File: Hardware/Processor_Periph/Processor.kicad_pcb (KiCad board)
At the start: 4 copper layers, 123.2 x 78.5 mm, 100 parts, among them J1 5V, J2 UART0, J3 USB_OTG, J4 JTAGICE3-SWD, J5 PIOA, J6 PIOB, J7 PIOC, J8 PIOD, Q1 BSSB06NE, Q2 BSSB06NE, Q3 BSSB06NE, Q4 BSSB06NE, SW1 PB, SW2 PB, SW3 ~RST, U1 TXS0102, U2 ATSAM4E16E, U3 3.0V, U4 LM3671, U5 PRTR5V0U2X, Y1 32.768kHz, Y2 12MHz

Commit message: Assigned some footprints, finished BOM
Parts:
- removed J1: 5V, FritzLib:ConnectorSMD-1x3
- removed J2: UART0, FritzLib:ConnectorSMD-1x4
- removed J3: USB_OTG, FritzLib:conn_usb_B_micro_smd
- removed J4: JTAGICE3-SWD, FritzLib:ConnectorMicromatch-10
- removed J5: PIOA, FritzLib:ConnectorSMD-40
- removed J6: PIOB, FritzLib:ConnectorSMD-24
- removed J7: PIOC, FritzLib:ConnectorSMD-40
- removed J8: PIOD, FritzLib:ConnectorSMD-40
- removed JP1: 5V_SEL, FritzLib:ConnectorSMD-1x3
- removed L1: 10uH, FritzLib:Inductor_3mmx3mm
- removed L2: 2.2uH, Inductors:Inductor_1212
- removed Q1, Q2, Q3, Q4: BSSB06NE, TO_SOT_Packages_SMD:SOT-23
- removed Y1: 32.768kHz, FritzLib:FC-135R
- removed Y2: 12MHz, Crystals:Crystal_HC49-SD_SMD
- added C29: 100nF, Capacitors_SMD:C_0603, F.Cu at (112.5, 75.4)
- added C42: 100nF, Capacitors_SMD:C_0603, F.Cu at (127.7, 74.7)
- added C43: 100nF, Capacitors_SMD:C_0603, F.Cu at (132.3, 69.8)
- added C44: 10uF, Capacitors_SMD:C_0805, F.Cu at (77.2, 104.0)
- added C45: 100nF, Capacitors_SMD:C_0603, F.Cu at (98.6, 103.1)
- added C46: 100nF, Capacitors_SMD:C_0603, F.Cu at (103.7, 98.1)
- added C47: 100nF, Capacitors_SMD:C_0603, F.Cu at (122.2, 70.0)
- added C48: 100nF, Capacitors_SMD:C_0603, F.Cu at (92.0, 106.1)
- added C49: 4.7uF, Capacitors_SMD:C_0805, F.Cu at (88.5, 94.1)
- added C50: 100nF, Capacitors_SMD:C_0603, F.Cu at (98.6, 98.1)
- added C51: 100nF, Capacitors_SMD:C_0603, F.Cu at (111.0, 86.7)
- added C52: 2.2uF, Capacitors_SMD:C_0805, F.Cu at (117.1, 64.8)
- added C53: 10uF, Capacitors_SMD:C_0805, F.Cu at (104.2, 77.7)
- added C54: 100nF, Capacitors_SMD:C_0603, F.Cu at (105.9, 93.0)
- added C55: 100nF, Capacitors_SMD:C_0603, F.Cu at (122.7, 74.9)
- added C56: 100nF, Capacitors_SMD:C_0603, F.Cu at (127.3, 69.8)
- added C57: 10nF, Capacitors_SMD:C_0603, F.Cu at (144.5, 64.8)
- added C58: 100nF, Capacitors_SMD:C_0603, F.Cu at (114.2, 80.3)
- added C59: 100nF, Capacitors_SMD:C_0603, F.Cu at (119.3, 80.1)
- added C60: 100nF, Capacitors_SMD:C_0603, F.Cu at (80.4, 114.4)
- added C61: 100nF, Capacitors_SMD:C_0603, F.Cu at (85.5, 109.5)
- added D6: PMEG6030ETP, FritzLib:SOD-128, F.Cu at (59.9, 114.4)
- added J10: JTAGICE3-SWD, Pin_Headers:Pin_Header_Straight_2x05_Pitch1.27mm_SMD, F.Cu at (77.3, 67.6)
- added R23: 100k, Resistors_SMD:R_0603, F.Cu at (141.0, 69.7)
- added R24: 0R, Resistors_SMD:R_0603, F.Cu at (102.0, 108.0)
- added R25: 2.2k, Resistors_SMD:R_0603, F.Cu at (134.4, 99.3)
- added R26: 10k, Resistors_SMD:R_0603, F.Cu at (147.9, 74.6)
- added R27: 0R, Resistors_SMD:R_0603, F.Cu at (127.5, 94.4)
- added R28: 10k, Resistors_SMD:R_0603, F.Cu at (119.9, 100.0)
- added R29: 2.2k, Resistors_SMD:R_0603, F.Cu at (144.4, 74.6)
- added R30: 27R, Resistors_SMD:R_0603, F.Cu at (105.5, 112.9)
- added R31: 27R, Resistors_SMD:R_0603, F.Cu at (112.7, 106.4)
- added R32: 27R, Resistors_SMD:R_0603, F.Cu at (124.0, 94.8)
- added R33: 27R, Resistors_SMD:R_0603, F.Cu at (120.6, 95.1)
- added R34: 0R, Resistors_SMD:R_0603, F.Cu at (132.7, 84.5)
- added R35: 0R, Resistors_SMD:R_0603, F.Cu at (137.5, 79.6)
- added R36: 1R, Resistors_SMD:R_0603, F.Cu at (124.0, 99.7)
- added R37: 10k, Resistors_SMD:R_0603, F.Cu at (108.9, 112.6)
- added R38: 1.5K, Resistors_SMD:R_0603, F.Cu at (137.5, 113.9)
- added R39: 10k, Resistors_SMD:R_0603, F.Cu at (141.6, 109.0)
- added R40: 10k, Resistors_SMD:R_0603, F.Cu at (145.2, 104.0)
- added R41: 10k, Resistors_SMD:R_0603, F.Cu at (138.2, 109.0)
- added R42: 27R, Resistors_SMD:R_0603, F.Cu at (133.3, 114.0)
- added R43: 10k, Resistors_SMD:R_0603, F.Cu at (141.6, 104.1)
- added R44: 10k, Resistors_SMD:R_0603, F.Cu at (145.2, 99.1)
- added R45: 10k, Resistors_SMD:R_0603, F.Cu at (130.0, 114.0)
- added R46: 10k, Resistors_SMD:R_0603, F.Cu at (138.2, 104.1)
- added R47: 10k, Resistors_SMD:R_0603, F.Cu at (133.9, 109.1)
- added R48: 10k, Resistors_SMD:R_0603, F.Cu at (136.3, 89.4)
- added R49: 2.2k, Resistors_SMD:R_0603, F.Cu at (127.4, 104.2)
- added R50: 2.2k, Resistors_SMD:R_0603, F.Cu at (139.8, 89.4)
- added R51: 2.2k, Resistors_SMD:R_0603, F.Cu at (134.7, 94.3)
- added R52: 2.2k, Resistors_SMD:R_0603, F.Cu at (119.5, 109.8)
- added R53: 150R, Resistors_SMD:R_0805, F.Cu at (91.1, 87.8)
- added R54: 2.2k, Resistors_SMD:R_0603, F.Cu at (112.4, 116.2)
- added R55: 2.2k, Resistors_SMD:R_0603, F.Cu at (123.4, 104.6)
- added R56: 2.2k, Resistors_SMD:R_0603, F.Cu at (142.9, 84.5)
- added R57: 2.2k, Resistors_SMD:R_0603, F.Cu at (131.0, 94.4)
- added R58: 10k, Resistors_SMD:R_0603, F.Cu at (116.0, 109.8)
- added R59: 150R, Resistors_SMD:R_0805, F.Cu at (100.0, 77.9)
- added R60: 2.2k, Resistors_SMD:R_0603, F.Cu at (136.2, 74.7)
- added R61: 2.2k, Resistors_SMD:R_0603, F.Cu at (127.4, 99.3)
- added R62: 2.2k, Resistors_SMD:R_0603, F.Cu at (144.6, 79.5)
- added R63: 2.2k, Resistors_SMD:R_0603, F.Cu at (119.5, 104.9)
- added R64: 10k, Resistors_SMD:R_0603, F.Cu at (139.4, 84.5)
- added R65: 2.2k, Resistors_SMD:R_0603, F.Cu at (112.5, 111.3)
- added R66: 2.2k, Resistors_SMD:R_0603, F.Cu at (108.9, 107.7)
- added R67: 2.2k, Resistors_SMD:R_0603, F.Cu at (141.0, 79.6)
- added R68: 2.2k, Resistors_SMD:R_0603, F.Cu at (132.8, 89.4)
- added R69: 150R, Resistors_SMD:R_0805, F.Cu at (95.6, 80.9)
- added R70: 10k, Resistors_SMD:R_0603, F.Cu at (136.0, 84.5)
- added R71: 10k, Resistors_SMD:R_0603, F.Cu at (116.0, 104.9)
- added R72: 2.2k, Resistors_SMD:R_0603, F.Cu at (145.1, 108.9)
- added R73: 2.2k, Resistors_SMD:R_0603, F.Cu at (130.4, 109.1)
- added R74: 2.2k, Resistors_SMD:R_0603, F.Cu at (141.7, 99.2)
- added R75: 2.2k, Resistors_SMD:R_0603, F.Cu at (146.5, 84.4)
- added R76: 150R, Resistors_SMD:R_0805, F.Cu at (112.6, 65.0)
- added R77: 2.2k, Resistors_SMD:R_0603, F.Cu at (134.7, 104.2)
- added R78: 2.2k, Resistors_SMD:R_0603, F.Cu at (138.1, 99.2)
- added R79: 2.2k, Resistors_SMD:R_0603, F.Cu at (123.1, 114.4)
- added R80: 2.2k, Resistors_SMD:R_0603, F.Cu at (131.1, 104.2)
- added R81: 27R, Resistors_SMD:R_0603, F.Cu at (146.7, 89.3)
- added R82: 27R, Resistors_SMD:R_0603, F.Cu at (141.5, 94.3)
- added R83: 27R, Resistors_SMD:R_0603, F.Cu at (126.9, 109.1)
- added R84: 27R, Resistors_SMD:R_0603, F.Cu at (146.7, 94.2)
- added R85: 27R, Resistors_SMD:R_0603, F.Cu at (119.3, 114.7)
- added R86: 27R, Resistors_SMD:R_0603, F.Cu at (138.2, 94.3)
- added R87: 27R, Resistors_SMD:R_0603, F.Cu at (143.3, 89.4)
- added R88: 27R, Resistors_SMD:R_0603, F.Cu at (123.0, 109.5)
- added R89: 27R, Resistors_SMD:R_0603, F.Cu at (130.9, 99.3)
- added R90: 27R, Resistors_SMD:R_0603, F.Cu at (116.0, 114.7)
- added R91: 27R, Resistors_SMD:R_0603, F.Cu at (148.1, 79.5)
- added R92: 0R, Resistors_SMD:R_0603, F.Cu at (126.6, 114.0)
- added TP10: 1V2, Measurement_Points:Test_Point_Keystone_5019_Minature, F.Cu at (86.4, 88.4)
- added TP11: XOUT_32, Measurement_Points:Test_Point_Keystone_5019_Minature, F.Cu at (93.8, 75.0)
- added TP12: XIN_32, Measurement_Points:Test_Point_Keystone_5019_Minature, F.Cu at (79.3, 98.3)
- added TP13: MCU_XIN, Measurement_Points:Test_Point_Keystone_5019_Minature, F.Cu at (90.0, 82.0)
- added TP14: PHY_XIN, Measurement_Points:Test_Point_Keystone_5019_Minature, F.Cu at (102.1, 65.6)
- added TP9: 1V8, Measurement_Points:Test_Point_Keystone_5019_Minature, F.Cu at (107.9, 65.6)
- added U7: DP83848C, Housings_QFP:LQFP-48_7x7mm_Pitch0.5mm, F.Cu at (53.5, 95.8)
- added U8: ATSAM4E16E, Housings_QFP:TQFP-144_20x20mm_Pitch0.5mm, F.Cu at (59.8, 75.6)
- added U9: 3.0V, TO_SOT_Packages_SMD:SOT-23, F.Cu at (88.5, 75.3)
- C10, C11: value 27pF -> 1uF; footprint Capacitors_SMD:C_0603 -> Capacitors_SMD:C_0805
- C13, C17, C22, C7: value 10nF -> 100nF
- C14, C16, C21, C33, C37: value 100nF -> 10nF
- C19, C20: value 12pF -> 100nF
- C2: value 10nF -> 4.7uF; footprint Capacitors_SMD:C_0603 -> Capacitors_SMD:C_0805
- C23: value 100nF -> 4.7uF; footprint Capacitors_SMD:C_0603 -> Capacitors_SMD:C_0805
- C31, C40: value 4.7uF -> 100nF; footprint Capacitors_SMD:C_0805 -> Capacitors_SMD:C_0603
- C34: value 2.2uF -> 100nF; footprint Capacitors_SMD:C_0805 -> Capacitors_SMD:C_0603
- C4: value 4.5nF -> 3.9pF
- C41: value 10uF -> 10nF; footprint Capacitors_SMD:C_0805 -> Capacitors_SMD:C_0603
- C5: value 100nF -> 3.9pF
- C6: value 100nF -> 4.5nF
- C9: value 100nF -> 10uF; footprint Capacitors_SMD:C_0603 -> Capacitors_SMD:C_0805
- D1, D2, D3, D4, D5: footprint LEDs:LED_0805 -> Diodes_SMD:D_0805
- R1: value 1M -> 10k; footprint Capacitors_SMD:C_0603 -> Resistors_SMD:R_0603
- R10, R9: value 10k -> 150R; footprint Capacitors_SMD:C_0603 -> Resistors_SMD:R_0805
- R11, R6: value 27R -> 10k; footprint Capacitors_SMD:C_0603 -> Resistors_SMD:R_0603
- R12, R18: value 10k -> 100k; footprint Capacitors_SMD:C_0603 -> Resistors_SMD:R_0603
- R13: value 10k -> 4.87k; footprint Capacitors_SMD:C_0603 -> Resistors_SMD:R_0603
- R14: value 150R -> 100k; footprint Capacitors_SMD:C_0805 -> Resistors_SMD:R_0603
- R15, R3, R4, R5: footprint Capacitors_SMD:C_0603 -> Resistors_SMD:R_0603
- R16, R20: value 10k -> 49.9R; footprint Capacitors_SMD:C_0603 -> Resistors_SMD:R_0603
- R17, R21: value 150R -> 49.9R; footprint Capacitors_SMD:C_0805 -> Resistors_SMD:R_0603
- R19, R22: value 150R -> 10k; footprint Capacitors_SMD:C_0805 -> Resistors_SMD:R_0603
- R2: value 10k -> 1M; footprint Capacitors_SMD:C_0603 -> Resistors_SMD:R_0603
- R7: value 27R -> 150R; footprint Capacitors_SMD:C_0603 -> Resistors_SMD:R_0805
- R8: value 1R -> 10k; footprint Capacitors_SMD:C_0603 -> Resistors_SMD:R_0603
- SW1: value PB -> ~RST
- SW3: value ~RST -> PB
- TP1: footprint Measurement_Points:Measurement_Point_Round-SMD-Pad_Small -> Measurement_Points:Test_Point_Keystone_5019_Minature
- TP2: value ERASE -> U0_RXD; footprint Measurement_Points:Measurement_Point_Round-SMD-Pad_Small -> Measurement_Points:Test_Point_Keystone_5019_Minature
- TP3: value U0_RXD -> LED_SPEED; footprint Measurement_Points:Measurement_Point_Round-SMD-Pad_Small -> Measurement_Points:Test_Point_Keystone_5019_Minature
- TP4: value JTAG_SEL -> ERASE; footprint Measurement_Points:Measurement_Point_Round-SMD-Pad_Small -> Measurement_Points:Test_Point_Keystone_5019_Minature
- TP5: value TST -> JTAG_SEL; footprint Measurement_Points:Measurement_Point_Round-SMD-Pad_Small -> Measurement_Points:Test_Point_Keystone_5019_Minature
- TP6: value 5V -> TST; footprint Measurement_Points:Measurement_Point_Round-SMD-Pad_Small -> Measurement_Points:Test_Point_Keystone_5019_Minature
- TP7: value 3V3 -> 5V; footprint Measurement_Points:Measurement_Point_Round-SMD-Pad_Small -> Measurement_Points:Test_Point_Keystone_5019_Minature
- TP8: value 1V2 -> 3V3; footprint Measurement_Points:Measurement_Point_Round-SMD-Pad_Small -> Measurement_Points:Test_Point_Keystone_5019_Minature
- U2: value ATSAM4E16E -> LM3671; footprint Housings_QFP:TQFP-144_20x20mm_Pitch0.5mm -> TO_SOT_Packages_SMD:SOT-23-5
- U3: value 3.0V -> S25FL127S; footprint TO_SOT_Packages_SMD:SOT-23 -> Housings_SOIC:SOIC-8_3.9x4.9mm_Pitch1.27mm
- U4: value LM3671 -> PRTR5V0U2X; footprint TO_SOT_Packages_SMD:SOT-23-5 -> TO_SOT_Packages_SMD:SOT-143
- U5: value PRTR5V0U2X -> MIC5365; footprint FritzLib:SOT143B -> TO_SOT_Packages_SMD:SOT-23-5
- moved TP4 308.4 mm to (60.6, 109.3)
- moved TP6 306.1 mm to (79.0, 91.9)
- moved TP3 301.2 mm to (72.1, 92.1)
- moved TP7 301.2 mm to (68.4, 101.5)
- moved TP1 299.8 mm to (66.1, 109.3)
- moved TP2 299.6 mm to (101.9, 72.0)
- moved TP8 293.1 mm to (81.3, 85.4)
- moved TP5 288.1 mm to (75.2, 85.4)
- moved D5 106.8 mm to (70.9, 113.8), turned to 0 degrees
- moved R10 104.6 mm to (73.0, 97.9), turned to 0 degrees
- moved U4 99.5 mm to (53.3, 106.2)
- moved SW3 93.0 mm to (87.5, 67.1)
- moved U1 83.1 mm to (95.4, 65.9), turned to 0 degrees
- moved U5 71.0 mm to (62.4, 102.2), turned to 0 degrees
- moved C15 69.8 mm to (100.8, 88.2)
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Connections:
- C1 pad 1: +3V3 -> +5V_UART
- C10 pad 1: /XIN32 -> +3V3
- C11 pad 1: /XOUT32 -> +1V8
- C12 pad 1: +1V2 -> +1V8
- C14 pad 1: +3V3 -> +1V8
- C16 pad 1: +1V2 -> +3V3
- C19 pad 1: /XOUT -> +3V3
- C2 pad 1: +3V3 -> +5V
- C20 pad 1: /XIN -> +1V2
- C21 pad 1: +1V2 -> +3V3
- C30 pad 1: /VDDPLL -> +3V3
- C31 pad 1: Net-(C31-Pad1) -> +3V3
- C32 pad 1: /AREF -> +1V2
- C34 pad 1: +1V2 -> +3V3
- C35 pad 1: +3V3 -> /PFBOUT
- C37 pad 1: Net-(C37-Pad1) -> +3V3
- C38 pad 1: /PE5 -> +3V3
- C39 pad 1: /PE4 -> /PFBOUT
- C4 pad 1: GND -> /XIN32
- C4 pad 2: Net-(C4-Pad2) -> GND
- C40 pad 1: +5V -> +1V2
- C5 pad 1: /VBUS -> /XOUT32
- C6 pad 1: +1V2 -> GND
- C6 pad 2: GND -> Net-(C6-Pad2)
- C7 pad 1: +3V3 -> +5V_USB
- C9 pad 1: +5V_UART -> +3V3
- D1 pad 1: Net-(D1-Pad1) -> GND
- D5 pad 1: GND -> Net-(D5-Pad1)
- R1 pad 1: GND -> +3V3
- R1 pad 2: Net-(C4-Pad2) -> /NVM_~CS
- R10 pad 1: +3V3 -> GND
- R10 pad 2: SWDCLK -> Net-(J4-Pad11)
- R11 pad 1: ~RST -> +1V8
- R11 pad 2: Net-(C37-Pad1) -> Net-(R11-Pad2)
- R12 pad 2: /PE5 -> /MCCDA2
- R13 pad 1: /PE0 -> /RBIAS
- R14 pad 2: Net-(D1-Pad2) -> /MCCDA3
- R15 pad 2: /PE4 -> /MCCDA
- R16 pad 1: /PE1 -> +3V3
- R16 pad 2: GND -> /ETX-
- R17 pad 1: +3V3 -> /ERX-
- R17 pad 2: Net-(D2-Pad2) -> +3V3
- R18 pad 1: /PE2 -> +3V3
- R18 pad 2: GND -> /MCDA0
- R19 pad 2: Net-(D3-Pad2) -> /I2C_SCL
- R2 pad 1: VBUS_DET -> GND
- R2 pad 2: /VBUS -> Net-(C6-Pad2)
- R20 pad 1: /PE3 -> +3V3
- R20 pad 2: GND -> /ETX+
- R21 pad 1: +3V3 -> /ERX-
- R21 pad 2: Net-(D4-Pad2) -> +3V3
- R22 pad 1: Net-(D5-Pad2) -> +3V3
- R22 pad 2: +3V3 -> /I2C_SCL
- R3 pad 2: Net-(R3-Pad2) -> +5V_USB
- R4 pad 1: Net-(R3-Pad2) -> VBUS_DET
- R4 pad 2: GND -> Net-(R4-Pad2)
- R5 pad 1: +3V3 -> Net-(R4-Pad2)
- R5 pad 2: /U0_TXD -> GND
- R6 pad 1: /DD- -> +3V3
- R6 pad 2: /USBD- -> /U0_TXD
- R7 pad 1: /DD+ -> Net-(D1-Pad2)
- R7 pad 2: /USBD+ -> +3V3
- R8 pad 1: /VDDPLL -> +3V3
- R8 pad 2: Net-(C31-Pad1) -> /LDO_EN
- R9 pad 1: +3V3 -> GND
- R9 pad 2: /AREF -> Net-(J4-Pad10)
- SW1 pad 1: /PE4 -> ~RST
- SW2 pad 1: /PE5 -> /SW2
- SW3 pad 1: ~RST -> /SW1
- TP2 pad 1: /ERASE -> /U0_RXD
- TP3 pad 1: /U0_RXD -> /LED_SP
- TP4 pad 1: /JTAG_SEL -> /ERASE
- TP5 pad 1: /TST -> /JTAG_SEL
- TP6 pad 1: +5V -> /TST
- TP7 pad 1: +3V3 -> +5V
- TP8 pad 1: +1V2 -> +3V3
- U2 pad 1: /PD0 -> +5V
- U2 pad 2: VBUS_DET -> GND
- U2 pad 3: +1V2 -> +5V
- U2 pad 4: /PE0 -> +3V3
- U2 pad 5: +3V3 -> Net-(L1-Pad1)
- U3 pad 1: /AREF -> /NVM_~CS
- U3 pad 2: GND -> /NVM_MISO
- U3 pad 3: (no net) -> Net-(U3-Pad3)
- U4 pad 1: +5V -> Net-(C6-Pad2)
- U4 pad 2: GND -> /USBD-
- U4 pad 3: +5V -> /USBD+
- U4 pad 4: +3V3 -> +5V_USB
- U5 pad 1: Net-(C4-Pad2) -> +3V3
- U5 pad 2: /USBD- -> GND
- U5 pad 3: /USBD+ -> /LDO_EN
- U5 pad 4: /VBUS -> Net-(U5-Pad4)
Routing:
- net /USBD-: track 17.3 -> 0.00 mm
- net /USBD+: track 17.3 -> 0.00 mm
- net /DD-: track 3.51 -> 0.00 mm
- net /DD+: track 3.47 -> 0.00 mm
- net GND: track 0.72 -> 0.00 mm
- removed copper zone on B.Cu, net GND
- removed copper zone on F.Cu, net GND
- removed copper zone on In1.Cu, net GND
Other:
- board size 123.2 x 78.5 mm -> 152.4 x 127 mm

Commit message: Started routing PHY
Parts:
- moved R84 276.8 mm to (-125.2, 146.3), turned to 270 degrees
- moved R81 275.7 mm to (-123.7, 143.5), turned to 90 degrees
- moved R91 275.7 mm to (-116.8, 155.7)
- moved R82 270.3 mm to (-123.7, 146.3), turned to 270 degrees
- moved R87 269.5 mm to (-120.7, 143.5), turned to 90 degrees
- moved R34 268.2 mm to (-128.3, 146.3), turned to 270 degrees
- moved R86 264.9 mm to (-122.2, 143.5), turned to 90 degrees
- moved R35 264.2 mm to (-116.8, 151.1), turned to 180 degrees
- moved R27 257.5 mm to (-121.2, 161.0), turned to 90 degrees
- moved R89 256.0 mm to (-120.7, 146.3), turned to 270 degrees
- moved R83 254.5 mm to (-125.2, 143.5), turned to 90 degrees
- moved C47 252.9 mm to (-116.8, 152.7)
- moved R88 247.9 mm to (-122.2, 146.3), turned to 270 degrees
- moved R85 240.6 mm to (-119.1, 146.3), turned to 90 degrees
- moved R90 236.2 mm to (-116.8, 154.2)
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
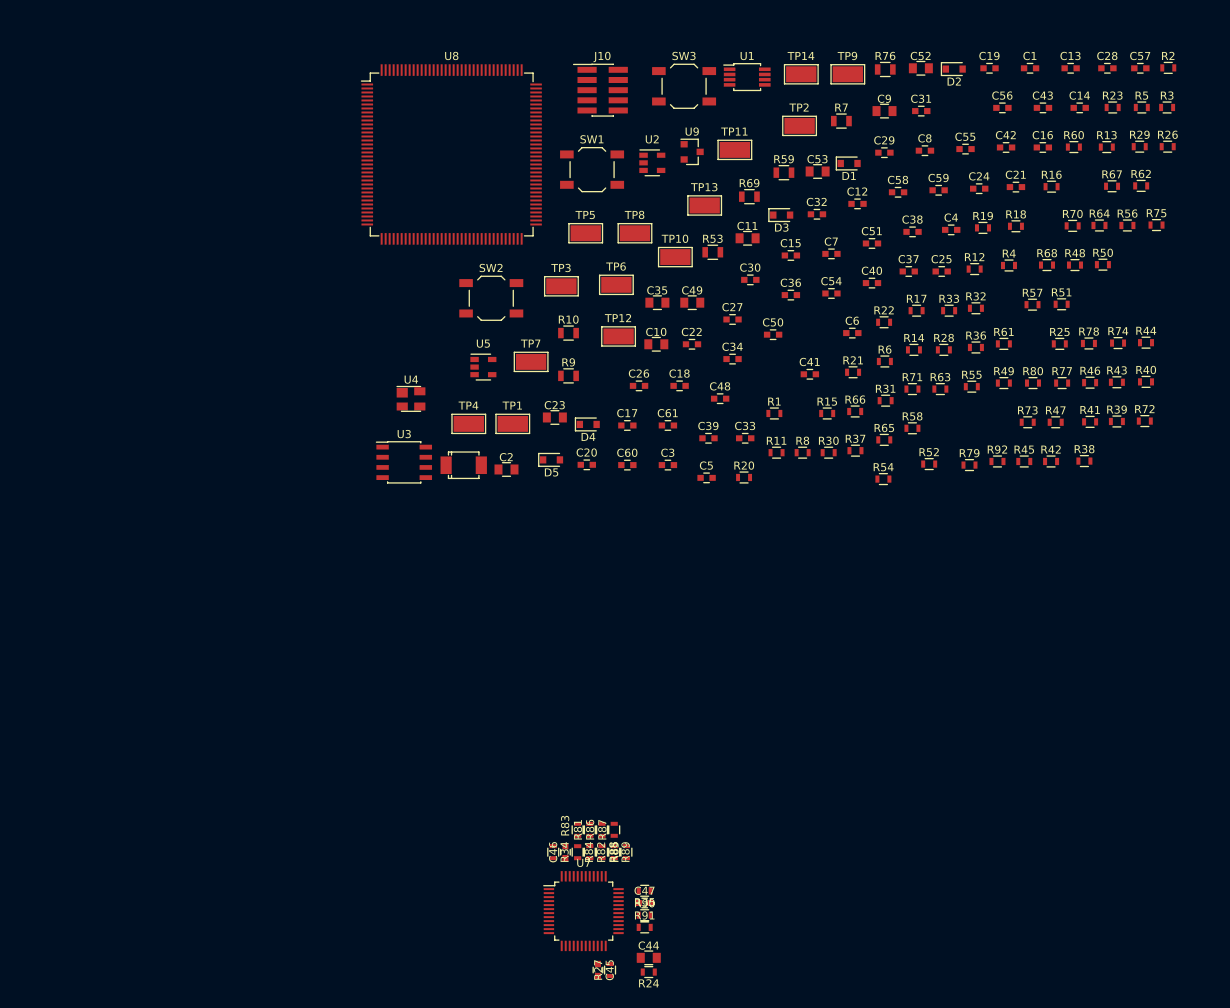
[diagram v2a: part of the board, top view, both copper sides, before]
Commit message: Modified schematic per 5/21 discussion
- Added 2xGPIO expanders & new connectors for interfacing to x4 stepper
motor drivers
- Added buffer for driving PWM outputs to stepper motors
- Added more spare pins & spare pin connectors
- Removed I2C expansion connector (I2C dedicated to GPIO expanders now)
- Cleaned up component values
- Expanded schematic size
- Reannotated entire schematic
- Regenerated schematic PDF

TODO:

- Generate new BOM with new schematic annotation
- Finalize connector footprints
- Begin layout
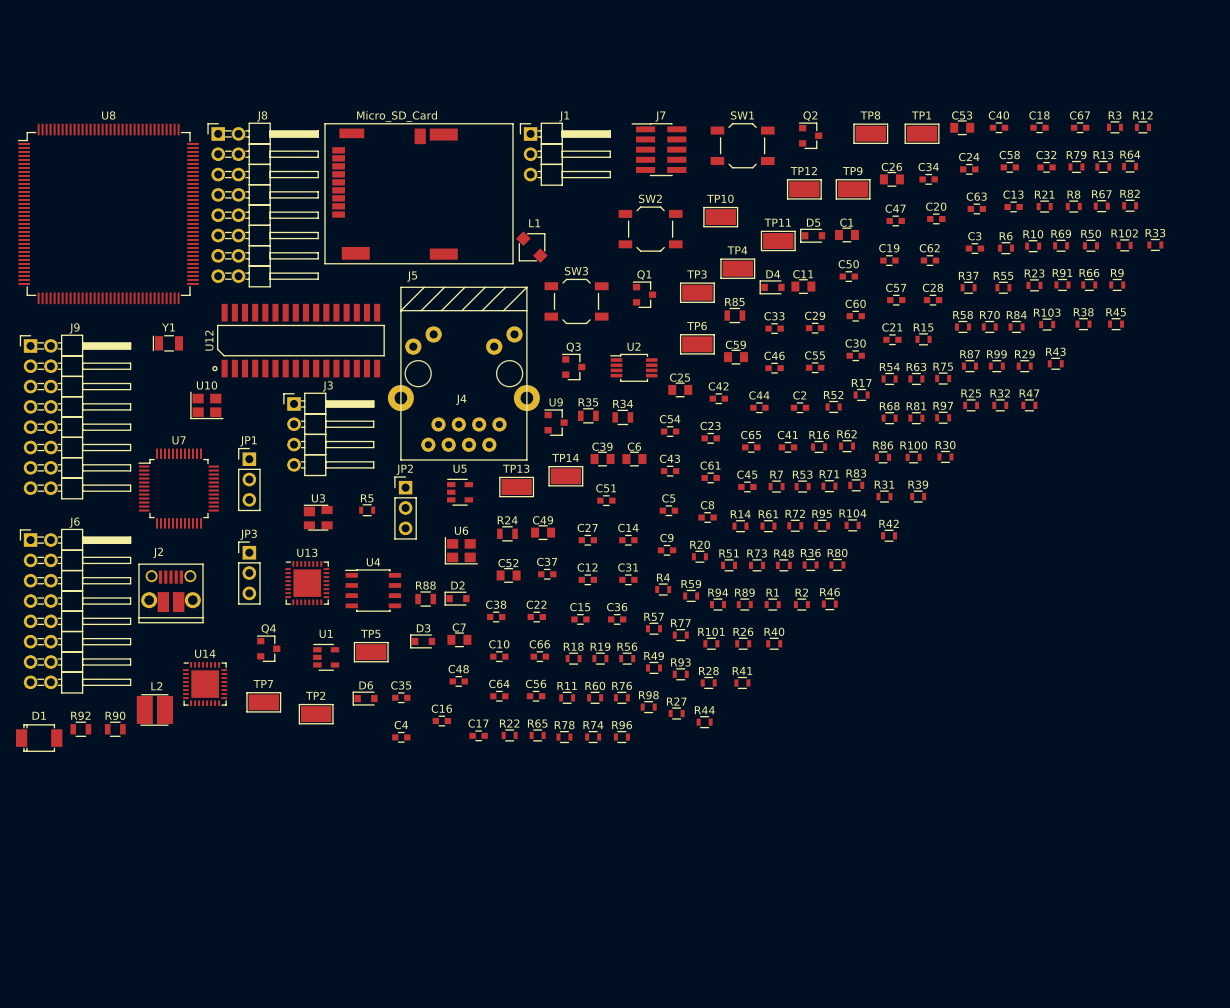
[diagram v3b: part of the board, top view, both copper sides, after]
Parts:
- removed J10: JTAGICE3-SWD, Pin_Headers:Pin_Header_Straight_2x05_Pitch1.27mm_SMD
- added C62: 100nF, Capacitors_SMD:C_0603, F.Cu at (-81.2, 72.3)
- added C63: 100nF, Capacitors_SMD:C_0603, F.Cu at (-75.3, 65.9)
- added C64: 100nF, Capacitors_SMD:C_0603, F.Cu at (-135.0, 126.8)
- added C65: 100nF, Capacitors_SMD:C_0603, F.Cu at (-103.5, 95.7)
- added C66: 100nF, Capacitors_SMD:C_0603, F.Cu at (-129.9, 121.9)
- added C67: 100nF, Capacitors_SMD:C_0603, F.Cu at (-62.4, 55.7)
- added J1: 5V, Pin_Headers:Pin_Header_Angled_1x03_Pitch2.54mm, F.Cu at (-131.1, 56.5)
- added J2: USB_OTG, FritzLib:USB_Micro-B_10103594-0001LF_holes, F.Cu at (-176.1, 113.4)
- added J3: UART0, Pin_Headers:Pin_Header_Angled_1x04_Pitch2.54mm, F.Cu at (-160.7, 90.3)
- added J4: RJ-45_J0006D01BNL, FritzLib:J0006D01BNL, F.Cu at (-147.3, 75.7)
- added J5: Micro_SD_Card, FritzLib:MicroSD-Yamaichi-PJS, F.Cu at (-154.3, 72.2)
- added J6: CONN_SPARE, Pin_Headers:Pin_Header_Angled_2x08_Pitch2.54mm, F.Cu at (-193.6, 107.3)
- added J7: JTAGICE3-SWD, Pin_Headers:Pin_Header_Straight_2x05_Pitch1.27mm_SMD, F.Cu at (-114.8, 58.5)
- added J8: CONN_SPARE, Pin_Headers:Pin_Header_Angled_2x08_Pitch2.54mm, F.Cu at (-170.2, 56.5)
- added J9: CONN_SPARE, Pin_Headers:Pin_Header_Angled_2x08_Pitch2.54mm, F.Cu at (-193.6, 83.0)
- added JP1: VCC_SEL, Pin_Headers:Pin_Header_Straight_1x03_Pitch2.54mm, F.Cu at (-166.3, 97.2)
- added JP2: VCC_SEL, Pin_Headers:Pin_Header_Straight_1x03_Pitch2.54mm, F.Cu at (-146.7, 100.7)
- added JP3: VCC_SEL, Pin_Headers:Pin_Header_Straight_1x03_Pitch2.54mm, F.Cu at (-166.3, 108.9)
- added L1: 2.2uH, FritzLib:CDRH2D14, F.Cu at (-131.9, 69.6)
- added L2: 10uH, FritzLib:Inductor_SMD_3.0mm_x_3.0mm, F.Cu at (-178.3, 128.5)
- added Q1: BSS806NE, TO_SOT_Packages_SMD:SOT-23, F.Cu at (-116.9, 76.6)
- added Q2: BSS806NE, TO_SOT_Packages_SMD:SOT-23, F.Cu at (-96.1, 56.7)
- added Q3: BSS806NE, TO_SOT_Packages_SMD:SOT-23, F.Cu at (-125.7, 85.7)
- added Q4: BSS806NE, TO_SOT_Packages_SMD:SOT-23, F.Cu at (-163.8, 120.9)
- added R100: 10k, Resistors_SMD:R_0603, F.Cu at (-83.2, 96.9)
- added R101: 10k, Resistors_SMD:R_0603, F.Cu at (-108.5, 120.2)
- added R102: 10k, Resistors_SMD:R_0603, F.Cu at (-56.8, 70.4)
- added R103: 10k, Resistors_SMD:R_0603, F.Cu at (-66.5, 80.3)
- added R104: 10k, Resistors_SMD:R_0603, F.Cu at (-90.8, 105.4)
- added R93: 10k, Resistors_SMD:R_0603, F.Cu at (-112.3, 124.1)
- added R94: 10k, Resistors_SMD:R_0603, F.Cu at (-107.7, 115.3)
- added R95: 10k, Resistors_SMD:R_0603, F.Cu at (-94.7, 105.5)
- added R96: 10k, Resistors_SMD:R_0603, F.Cu at (-119.7, 131.9)
- added R97: 10k, Resistors_SMD:R_0603, F.Cu at (-79.5, 92.0)
- added R98: 10k, Resistors_SMD:R_0603, F.Cu at (-116.3, 128.2)
- added R99: 10k, Resistors_SMD:R_0603, F.Cu at (-72.8, 85.5)
- added U10: ASE-25.000MHZ-LC-T, Crystals:Crystal_SMD_3225-4pin_3.2x2.5mm, F.Cu at (-171.6, 90.4)
- added U12: CY7C1018, FritzLib:32-SOJ-300mil, F.Cu at (-159.8, 82.4)
- added U13: TCA6424A, Housings_DFN_QFN:QFN-32-1EP_5x5mm_Pitch0.5mm, F.Cu at (-159.0, 112.7)
- added U14: TCA6424A, Housings_DFN_QFN:QFN-32-1EP_5x5mm_Pitch0.5mm, F.Cu at (-171.8, 125.3)
- added U6: DSC61XX, Crystals:Crystal_SMD_3225-4pin_3.2x2.5mm, F.Cu at (-139.8, 108.6)
- added Y1: 32.768kHz, Crystals:Crystal_SMD_MicroCrystal_CC7V-T1A-2pin_3.2x1.5mm, F.Cu at (-176.3, 82.7)
- C1, C59: value 100nF -> 4.7uF; footprint Capacitors_SMD:C_0603 -> Capacitors_SMD:C_0805
- C10: value 1uF -> 100nF; footprint Capacitors_SMD:C_0805 -> Capacitors_SMD:C_0603
- C13, C17, C32, C36, C45, C56: value 100nF -> 10nF
- C14, C16, C33, C37, C57: value 10nF -> 100nF
- C2, C23: value 4.7uF -> 100nF; footprint Capacitors_SMD:C_0805 -> Capacitors_SMD:C_0603
- C25: value 10nF -> 4.7uF; footprint Capacitors_SMD:C_0603 -> Capacitors_SMD:C_0805
- C26, C39, C7: value 100nF -> 10uF; footprint Capacitors_SMD:C_0603 -> Capacitors_SMD:C_0805
- C3: value 100nF -> 4.5nF
- C35, C44: value 10uF -> 100nF; footprint Capacitors_SMD:C_0805 -> Capacitors_SMD:C_0603
- C4, C5: value 3.9pF -> 100nF
- C6: value 4.5nF -> 1uF; footprint Capacitors_SMD:C_0603 -> Capacitors_SMD:C_0805
- C8: value 100nF -> 3.9pF
- C9: value 10uF -> 3.9pF; footprint Capacitors_SMD:C_0805 -> Capacitors_SMD:C_0603
- D1: value LED -> PMEG6030ETP; footprint Diodes_SMD:D_0805 -> FritzLib:SOD-128
- D6: value PMEG6030ETP -> LED; footprint FritzLib:SOD-128 -> Diodes_SMD:D_0805
- R1, R11, R15, R22, R26, R28, R3, R4, R47, R8: value 10k -> 2.2k
- R10, R9: value 150R -> 2.2k; footprint Resistors_SMD:R_0805 -> Resistors_SMD:R_0603
- R12, R18: value 100k -> 10k
- R13: value 4.87k -> 10k
- R14, R23: value 100k -> 2.2k
- R16, R17, R20, R21: value 49.9R -> 2.2k
- R2: value 1M -> 2.2k
- R24, R34, R35, R92: value 0R -> 150R; footprint Resistors_SMD:R_0603 -> Resistors_SMD:R_0805
- R27: value 0R -> 2.2k
- R30, R31, R32: value 27R -> 2.2k
- R33, R81, R82, R83, R84, R86, R87, R89, R91: value 27R -> 10k
- R36: value 1R -> 0R
- R37: value 10k -> 4.87k
- R38: value 1.5K -> 49.9R
- R39, R41: value 10k -> 49.9R
- R40, R43: value 10k -> 100k
- R42: value 27R -> 49.9R
- R45: value 10k -> 0R
- R49, R56: value 2.2k -> 0R
- R5: value 10k -> 1M
- R50, R55: value 2.2k -> 100k
- R52, R54, R73, R75, R77, R79, R80: value 2.2k -> 10k
- R53: value 150R -> 0R; footprint Resistors_SMD:R_0805 -> Resistors_SMD:R_0603
- R57, R60, R61, R62, R63, R65, R66, R67, R68, R78: value 2.2k -> 27R
- R58, R64, R70, R71: value 10k -> 27R
- R59, R69: value 150R -> 27R; footprint Resistors_SMD:R_0805 -> Resistors_SMD:R_0603
- R7, R76: value 150R -> 10k; footprint Resistors_SMD:R_0805 -> Resistors_SMD:R_0603
- R72: value 2.2k -> 1R
- R74: value 2.2k -> 1.5K
- R85, R88, R90: value 27R -> 150R; footprint Resistors_SMD:R_0603 -> Resistors_SMD:R_0805
- SW1: value ~RST -> PB
- TP1, TP2: footprint Measurement_Points:Test_Point_Keystone_5019_Minature -> FritzLib:Test_Point_Keystone_5019_Minature
- TP10: value 1V2 -> LED_SPEED; footprint Measurement_Points:Test_Point_Keystone_5019_Minature -> FritzLib:Test_Point_Keystone_5019_Minature
- TP11: value XOUT_32 -> ERASE; footprint Measurement_Points:Test_Point_Keystone_5019_Minature -> FritzLib:Test_Point_Keystone_5019_Minature
- TP12: value XIN_32 -> PHY_XIN; footprint Measurement_Points:Test_Point_Keystone_5019_Minature -> FritzLib:Test_Point_Keystone_5019_Minature
- TP13: value MCU_XIN -> JTAG_SEL; footprint Measurement_Points:Test_Point_Keystone_5019_Minature -> FritzLib:Test_Point_Keystone_5019_Minature
- TP14: value PHY_XIN -> TST; footprint Measurement_Points:Test_Point_Keystone_5019_Minature -> FritzLib:Test_Point_Keystone_5019_Minature
- TP3: value LED_SPEED -> 5V; footprint Measurement_Points:Test_Point_Keystone_5019_Minature -> FritzLib:Test_Point_Keystone_5019_Minature
- TP4: value ERASE -> 3V3; footprint Measurement_Points:Test_Point_Keystone_5019_Minature -> FritzLib:Test_Point_Keystone_5019_Minature
- TP5: value JTAG_SEL -> 1V8; footprint Measurement_Points:Test_Point_Keystone_5019_Minature -> FritzLib:Test_Point_Keystone_5019_Minature
- TP6: value TST -> 1V2; footprint Measurement_Points:Test_Point_Keystone_5019_Minature -> FritzLib:Test_Point_Keystone_5019_Minature
- TP7: value 5V -> XOUT_32; footprint Measurement_Points:Test_Point_Keystone_5019_Minature -> FritzLib:Test_Point_Keystone_5019_Minature
- TP8: value 3V3 -> MCU_XIN; footprint Measurement_Points:Test_Point_Keystone_5019_Minature -> FritzLib:Test_Point_Keystone_5019_Minature
- TP9: value 1V8 -> XIN_32; footprint Measurement_Points:Test_Point_Keystone_5019_Minature -> FritzLib:Test_Point_Keystone_5019_Minature
- U1: value TXS0102 -> LM3671; footprint Housings_SSOP:MSOP-8_3x3mm_Pitch0.65mm -> TO_SOT_Packages_SMD:SOT-23-5
- U2: value LM3671 -> TXS0102; footprint TO_SOT_Packages_SMD:SOT-23-5 -> Housings_SSOP:MSOP-8_3x3mm_Pitch0.65mm
- U3: value S25FL127S -> PRTR5V0U2X; footprint Housings_SOIC:SOIC-8_3.9x4.9mm_Pitch1.27mm -> TO_SOT_Packages_SMD:SOT-143
- U4: value PRTR5V0U2X -> S25FL127S; footprint TO_SOT_Packages_SMD:SOT-143 -> Housings_SOIC:SOIC-8_3.9x4.9mm_Pitch1.27mm
- moved D1 124.1 mm to (-192.5, 132.0)
- moved R92 119.4 mm to (-187.3, 130.9)
- moved R5 109.1 mm to (-151.5, 103.6)
- moved R82 105.3 mm to (-56.2, 65.5), turned to 0 degrees
- moved C16 103.8 mm to (-142.2, 129.9)
- moved R91 95.8 mm to (-64.6, 75.4)
- moved TP2 95.2 mm to (-157.9, 129.0)
- moved C56 93.8 mm to (-130.4, 126.8)
- moved C4 93.5 mm to (-147.3, 131.9)
- moved R60 91.2 mm to (-123.0, 127.0)
- moved C47 90.8 mm to (-85.5, 67.4)
- moved D2 90.7 mm to (-140.2, 114.6)
- moved U1 89.6 mm to (-156.7, 121.9)
- moved R84 85.6 mm to (-70.4, 80.6), turned to 0 degrees
- moved R76 85.2 mm to (-119.7, 127.0)
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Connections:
- C1 pad 1: +5V_UART -> +5V
- C13 pad 1: +3V3 -> +1V8
- C14 pad 1: +1V8 -> +3V3
- C2 pad 1: +5V -> +5V_UART
- C24 pad 1: +1V2 -> +3V3
- C26 pad 1: +3V3 -> /PFBOUT
- C3 pad 1: +3V3 -> GND
- C3 pad 2: GND -> Net-(C3-Pad2)
- C30 pad 1: +3V3 -> /PFBOUT
- C31 pad 1: +3V3 -> +1V2
- C32 pad 1: +1V2 -> +3V3
- C34 pad 1: +3V3 -> /PFBIN1
- C35 pad 1: /PFBOUT -> +1V2
- C36 pad 1: +1V2 -> +3V3
- C38 pad 1: +3V3 -> /PFBIN2
- C39 pad 1: /PFBOUT -> Net-(C39-Pad1)
- C4 pad 1: /XIN32 -> +3V3
- C42 pad 1: /PFBIN1 -> +3V3
- C43 pad 1: /PFBIN2 -> Net-(C39-Pad1)
- C44 pad 1: Net-(C44-Pad1) -> +1V2
- C45 pad 1: Net-(C44-Pad1) -> +3V3
- C46 pad 1: Net-(C44-Pad1) -> Net-(C39-Pad1)
- C47 pad 1: Net-(C44-Pad1) -> Net-(C39-Pad1)
- C5 pad 1: /XOUT32 -> +5V_USB
- C54 pad 1: +1V2 -> +3V3
- C55 pad 1: +3V3 -> +1V2
- C56 pad 1: ~RST -> +3V3
- C58 pad 1: /SW2 -> /~RST
- C59 pad 1: /SW1 -> +3V3
- C6 pad 1: GND -> +3V3
- C6 pad 2: Net-(C6-Pad2) -> GND
- C60 pad 1: +3V3 -> /SW2
- C61 pad 1: +3V3 -> /SW1
- C7 pad 1: +5V_USB -> +3V3
- C8 pad 1: +3V3 -> /XIN32
- C9 pad 1: +3V3 -> /XOUT32
- D1 pad 1: GND -> +5V_EXT
- D2 pad 1: Net-(D2-Pad1) -> GND
- D6 pad 1: +5V_EXT -> Net-(D6-Pad1)
- R1 pad 2: /NVM_~CS -> /GCOL
- R10 pad 1: GND -> +3V3
- R10 pad 2: Net-(J4-Pad11) -> /LED_LN
- R11 pad 1: +1V8 -> /LED_LN
- R11 pad 2: Net-(R11-Pad2) -> GND
- R12 pad 1: +3V3 -> /VBUS_DET
- R12 pad 2: /MCCDA2 -> Net-(R12-Pad2)
- R13 pad 1: /RBIAS -> Net-(R12-Pad2)
- R14 pad 2: /MCCDA3 -> /GRX1
- R15 pad 1: +3V3 -> /GRX1
- R15 pad 2: /MCCDA -> GND
- R16 pad 2: /ETX- -> /LED_SP
- R17 pad 1: /ERX- -> /LED_SP
- R17 pad 2: +3V3 -> GND
- R18 pad 2: /MCDA0 -> /LDO_EN
- R19 pad 2: /I2C_SCL -> /U0_TXD
- R2 pad 1: GND -> /GCOL
- R2 pad 2: Net-(C6-Pad2) -> GND
- R20 pad 2: /ETX+ -> /GRX2
- R21 pad 1: /ERX- -> /GRX2
- R21 pad 2: +3V3 -> GND
- R22 pad 2: /I2C_SCL -> /GRXDV
- R23 pad 1: +3V3 -> /GRXDV
- R23 pad 2: /MCDA1 -> GND
- R24 pad 1: +3V3 -> Net-(D2-Pad2)
- R24 pad 2: Net-(C44-Pad1) -> +3V3
- R25 pad 1: Net-(R25-Pad1) -> +3V3
- R25 pad 2: +3V3 -> /GRX3
- R26 pad 1: +3V3 -> /GRX3
- R26 pad 2: /I2C_SDA -> GND
- R27 pad 2: Net-(C44-Pad1) -> /GTX3
- R28 pad 1: +3V3 -> /GTX3
- R28 pad 2: /I2C_SDA -> GND
- R29 pad 1: Net-(R29-Pad1) -> +3V3
- R29 pad 2: +3V3 -> /GCRS
- R3 pad 1: VBUS_DET -> +3V3
- R3 pad 2: +5V_USB -> /LED_ACT
- R30 pad 1: /NVM_SCK_R -> /GCRS
- R30 pad 2: /NVM_SCK -> GND
- R31 pad 1: /MCCK_R -> +3V3
- R31 pad 2: /MCCK -> /GRXER
- R32 pad 1: /USBD_R- -> /GRXER
- R32 pad 2: /USBD- -> GND
- R33 pad 1: /USBD_R+ -> +1V8
- R33 pad 2: /USBD+ -> Net-(R33-Pad2)
- R34 pad 1: +3V3 -> GND
- R34 pad 2: Net-(C44-Pad1) -> Net-(J4-Pad10)
- R35 pad 1: +3V3 -> GND
- R35 pad 2: Net-(C44-Pad1) -> Net-(J4-Pad11)
- R36 pad 1: /VDDPLL -> +3V3
- R36 pad 2: Net-(C49-Pad1) -> +1V8
- R37 pad 1: +3V3 -> /RBIAS
- R37 pad 2: /AREF -> GND
- R38 pad 2: /GMDIO -> /ETX-
- R39 pad 1: +3V3 -> /ERX-
- R39 pad 2: /PHY_~INT -> +3V3
- R4 pad 1: VBUS_DET -> /LED_ACT
- R4 pad 2: Net-(R4-Pad2) -> GND
- R40 pad 2: /PHY_~RST -> /MCCDA2
- R41 pad 2: Net-(R41-Pad2) -> /ETX+
- R42 pad 1: ~RST -> /ERX-
- R42 pad 2: /~RST_R -> +3V3
- R43 pad 2: /RAM_~RD -> /MCCDA3
- R44 pad 2: /RAM_~WE -> /I2C_SCL
- R45 pad 2: /RAM_~CS -> Net-(C39-Pad1)
- R46 pad 2: /SW2 -> /I2C_SCL
- R47 pad 1: +3V3 -> Net-(R47-Pad1)
- R47 pad 2: /SW1 -> +3V3
- R48 pad 1: /LED1 -> +3V3
- R48 pad 2: GND -> /MCCDA
- R49 pad 2: /GCOL -> Net-(C39-Pad1)
- R5 pad 1: Net-(R4-Pad2) -> GND
- R5 pad 2: GND -> Net-(C3-Pad2)
- R50 pad 1: /GCOL -> +3V3
- R50 pad 2: GND -> /MCDA0
- R51 pad 1: +3V3 -> Net-(R51-Pad1)
- R51 pad 2: /LED_ACT -> +3V3
- R52 pad 1: /LED_ACT -> +3V3
- R52 pad 2: GND -> /I2C_SDA
- R53 pad 2: Net-(D2-Pad2) -> Net-(C39-Pad1)
- R54 pad 2: /GRX0 -> /I2C_SDA
- R55 pad 1: /GRX0 -> +3V3
- R55 pad 2: GND -> /MCDA1
- R56 pad 2: /LED_LN -> Net-(C39-Pad1)
- R57 pad 1: /LED_LN -> /NVM_SCK_R
- R57 pad 2: GND -> /NVM_SCK
- R58 pad 1: /LED2 -> /MCCK_R
- R58 pad 2: GND -> /MCCK
- R59 pad 1: +3V3 -> /USBD_R-
- R59 pad 2: Net-(D3-Pad2) -> /USBD-
- R6 pad 2: /U0_TXD -> /NVM_~CS
- R60 pad 1: +3V3 -> /USBD_R+
- R60 pad 2: /GRX1 -> /USBD+
- R61 pad 1: /GRX1 -> /GRX0
- R61 pad 2: GND -> /GRX0_R
- R62 pad 1: +3V3 -> /GRX1
- R62 pad 2: /LED_SP -> /GRX1_R
- R63 pad 1: /LED_SP -> /GRX2
- R63 pad 2: GND -> /GRX2_R
- R64 pad 1: /LED3 -> /GRX3
- R64 pad 2: GND -> /GRX3_R
- R65 pad 1: +3V3 -> /GRXCK
- R65 pad 2: /GRX2 -> /GRXCK_R
- R66 pad 1: /GRX2 -> /GRXER
- R66 pad 2: GND -> /GRXER_R
- R67 pad 1: +3V3 -> /GRXDV
- R67 pad 2: /GRXDV -> /GRXDV_R
- R68 pad 1: /GRXDV -> /GCOL
- R68 pad 2: GND -> /GCOL_R
- R69 pad 1: +3V3 -> /GCRS
- R69 pad 2: Net-(D4-Pad2) -> /GCRS_R
- R7 pad 1: Net-(D1-Pad2) -> /VBUS_DET
- R7 pad 2: +3V3 -> +5V_USB
- R70 pad 1: +3V3 -> /GMDC
- R70 pad 2: SWDCLK -> /GMDC_R
- R71 pad 1: /LED4 -> /GMDIO
- R71 pad 2: GND -> /GMDIO_R
- R72 pad 1: +3V3 -> /VDDPLL
- R72 pad 2: /GRX3 -> Net-(C49-Pad1)
- R73 pad 1: /GRX3 -> +3V3
- R73 pad 2: GND -> /AREF
- R74 pad 2: /GTX3 -> /GMDIO
- R75 pad 1: /GTX3 -> +3V3
- R75 pad 2: GND -> /PHY_~INT
- R76 pad 2: Net-(D5-Pad2) -> Net-(R76-Pad2)
- R77 pad 2: /GCRS -> /PHY_~RST
- R78 pad 1: /GCRS -> /~RST
- R78 pad 2: GND -> /~RST_R
- R79 pad 2: /GRXER -> /SW2
- R8 pad 2: /LDO_EN -> /GRX0
- R80 pad 1: /GRXER -> +3V3
- R80 pad 2: GND -> /SW1
- R81 pad 1: /GRX0 -> +3V3
- R81 pad 2: /GRX0_R -> /RAM_~RD
- R82 pad 1: /GRX1 -> +3V3
- R82 pad 2: /GRX1_R -> /RAM_~WE
- R83 pad 1: /GRX2 -> +3V3
- R83 pad 2: /GRX2_R -> /RAM_~CS
- R84 pad 1: /GRX3 -> /LED1
- R84 pad 2: /GRX3_R -> GND
- R85 pad 1: /GRXCK -> +3V3
- R85 pad 2: /GRXCK_R -> Net-(D3-Pad2)
- R86 pad 1: /GRXER -> +3V3
- R86 pad 2: /GRXER_R -> /SWDCLK
- R87 pad 1: /GRXDV -> /LED2
- R87 pad 2: /GRXDV_R -> GND
- R88 pad 1: /GCOL -> +3V3
- R88 pad 2: /GCOL_R -> Net-(D4-Pad2)
- R89 pad 1: /GCRS -> /LED3
- R89 pad 2: /GCRS_R -> GND
- R9 pad 1: GND -> /GRX0
- R9 pad 2: Net-(J4-Pad10) -> GND
- R90 pad 1: /GMDC -> +3V3
- R90 pad 2: /GMDC_R -> Net-(D5-Pad2)
- R91 pad 1: /GMDIO -> /LED4
- R91 pad 2: /GMDIO_R -> GND
- R92 pad 2: +1V8 -> Net-(D6-Pad2)
- SW1 pad 1: ~RST -> /~RST
- TP10 pad 1: +1V2 -> /LED_SP
- TP11 pad 1: /XOUT32 -> /ERASE
- TP12 pad 1: /XIN32 -> /PHY_XIN
- TP13 pad 1: /MCU_XIN -> /JTAG_SEL
- TP14 pad 1: /PHY_XIN -> /TST
- TP3 pad 1: /LED_SP -> +5V
- TP4 pad 1: /ERASE -> +3V3
- TP5 pad 1: /JTAG_SEL -> +1V8
- TP6 pad 1: /TST -> +1V2
- TP7 pad 1: +5V -> /XOUT32
- TP8 pad 1: +3V3 -> /MCU_XIN
- TP9 pad 1: +1V8 -> /XIN32
- U1 pad 1: /UART_RXD -> +5V
- U1 pad 3: +3V3 -> +5V
- U1 pad 4: /U0_TXD -> +3V3
- U1 pad 5: /U0_RXD -> Net-(L1-Pad1)
- U2 pad 1: +5V -> /UART_RXD
- U2 pad 3: +5V -> +3V3
- U2 pad 4: +3V3 -> /U0_TXD
- U2 pad 5: Net-(L1-Pad1) -> /U0_RXD
- U3 pad 1: /NVM_~CS -> Net-(C3-Pad2)
- U3 pad 2: /NVM_MISO -> /USBD-
- U3 pad 3: Net-(U3-Pad3) -> /USBD+
- U3 pad 4: GND -> +5V_USB
- U4 pad 1: Net-(C6-Pad2) -> /NVM_~CS
- U4 pad 2: /USBD- -> /NVM_MISO
- U4 pad 3: /USBD+ -> Net-(U4-Pad3)
- U4 pad 4: +5V_USB -> GND
- U7 pad 20: Net-(R29-Pad1) -> Net-(R51-Pad1)
- U7 pad 21: Net-(R25-Pad1) -> Net-(R47-Pad1)
- U7 pad 22: Net-(C44-Pad1) -> Net-(C39-Pad1)
- U7 pad 32: Net-(C44-Pad1) -> Net-(C39-Pad1)
- U7 pad 48: Net-(C44-Pad1) -> Net-(C39-Pad1)
- U8 pad 109: SWO -> /SWO
- U8 pad 114: /PA6 -> /GPIO_23_~RST
- U8 pad 2: VBUS_DET -> /VBUS_DET
- U8 pad 73: /PA5 -> /GPIO_23_~INT
- U8 pad 79: SWDIO -> /SWDIO
- U8 pad 89: SWDCLK -> /SWDCLK
- U8 pad 93: /PA2 -> /GPIO_01_~RST
- U8 pad 99: /PA1 -> /GPIO_01_~INT
